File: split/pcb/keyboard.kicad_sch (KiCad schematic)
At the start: 116 parts, among them J1 TRRS, J2 IO

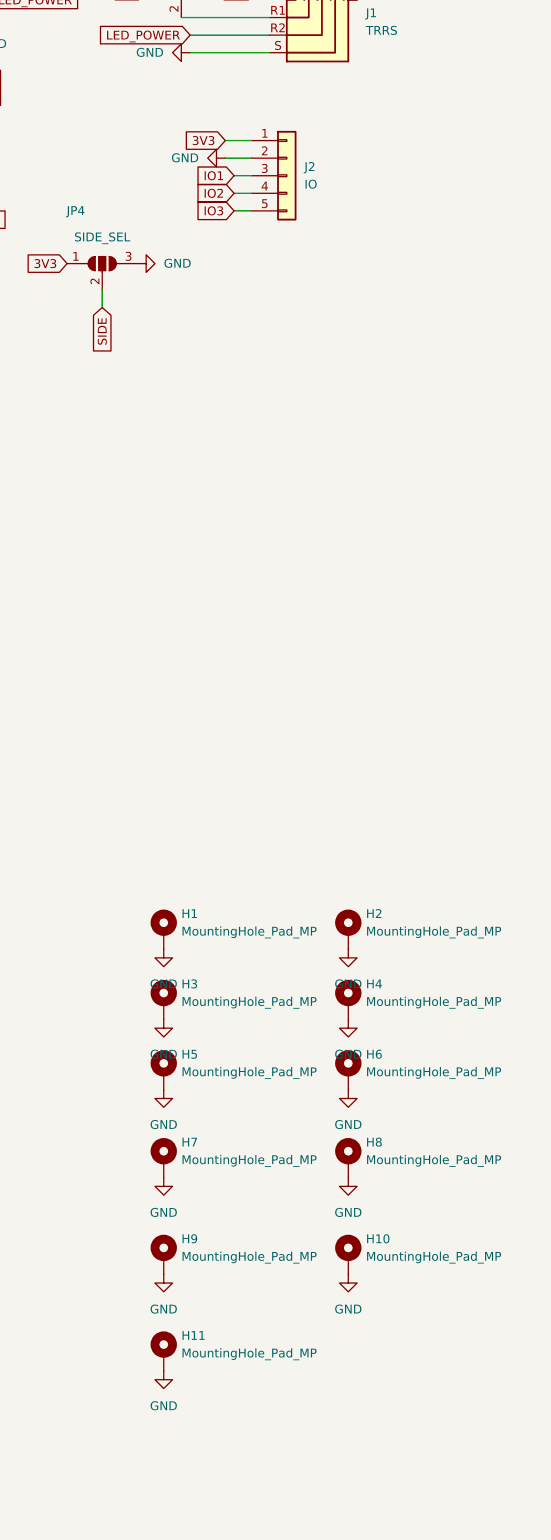
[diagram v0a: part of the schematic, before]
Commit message: fix accessory connector
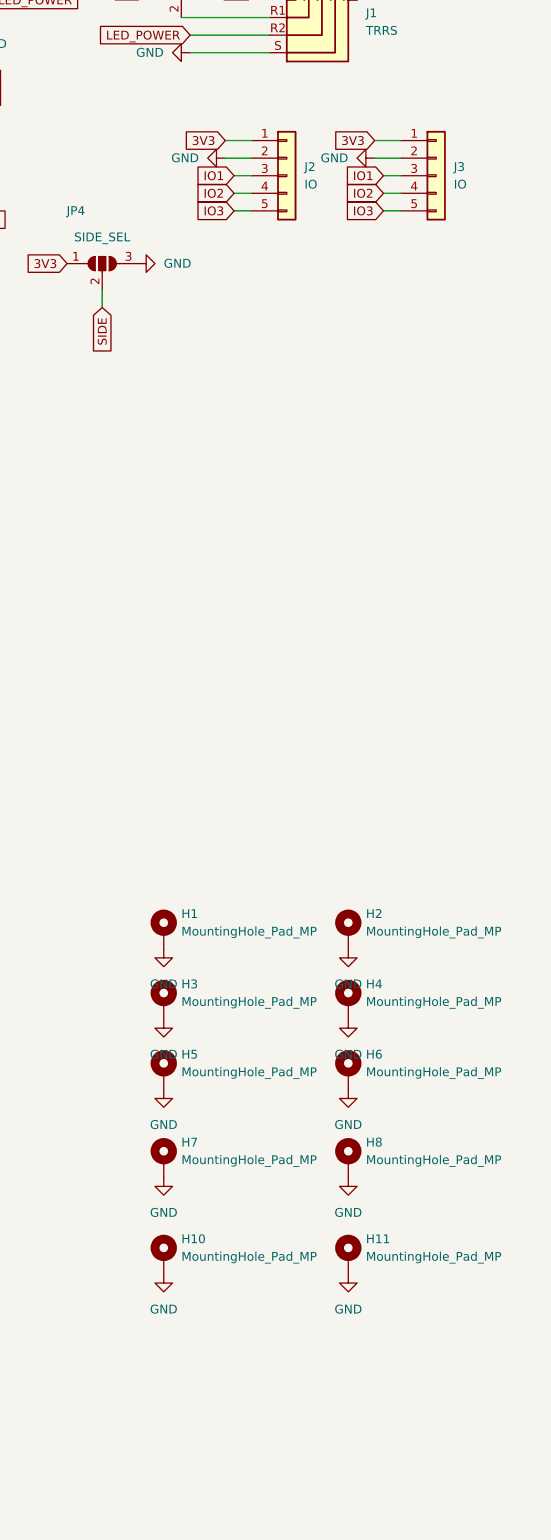
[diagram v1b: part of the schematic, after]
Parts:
- removed H9: MountingHole_Pad_MP, MountingHole:MountingHole_2.2mm_M2_DIN965_Pad, symbol Mechanical:MountingHole_Pad
- added J3: IO, Connector_PinHeader_2.54mm:PinHeader_1x05_P2.54mm_Vertical, symbol Connector_Generic:Conn_01x05
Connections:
- net 3V3: now also J3.1 (Pin_1)
- net GND: now also J3.2 (Pin_2)
- net IO1: now also J3.3 (Pin_3)
- net IO2: now also J3.4 (Pin_4)
- net IO3: now also J3.5 (Pin_5)
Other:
- moved on the sheet: H10, H11

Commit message: pcb fixes
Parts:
- removed JP2: T_SEL, Jumper:SolderJumper-3_P1.3mm_Open_Pad1.0x1.5mm, symbol Jumper:SolderJumper_3_Open
- removed JP3: R1_SEL, Jumper:SolderJumper-3_P1.3mm_Open_Pad1.0x1.5mm, symbol Jumper:SolderJumper_3_Open
- added JP1: SolderJumper_2_Open, Jumper:SolderJumper-2_P1.3mm_Open_Pad1.0x1.5mm, symbol Jumper:SolderJumper_2_Open
- J2, J3: footprint Connector_PinHeader_2.54mm:PinHeader_1x05_P2.54mm_Vertical -> Connector_PinHeader_2.54mm:PinHeader_1x07_P2.54mm_Vertical; symbol Connector_Generic:Conn_01x05 -> Connector_Generic:Conn_01x07
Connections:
- net GND: now also J2.3 (Pin_3), J3.3 (Pin_3), JP1.2 (B); no longer J2.2 (Pin_2), J3.2 (Pin_2)
- net IO1: now also J2.4 (Pin_4), J3.4 (Pin_4); no longer J2.3 (Pin_3), J3.3 (Pin_3)
- net IO2: now also J2.5 (Pin_5), J3.5 (Pin_5); no longer J2.4 (Pin_4), J3.4 (Pin_4)
- net IO3: now also J2.6 (Pin_6), J3.6 (Pin_6); no longer J2.5 (Pin_5), J3.5 (Pin_5)
- net LED_POWER: now also J2.2 (Pin_2), J3.2 (Pin_2)
- net RX: now also J1.R1
- net TX: now also J1.T
- net IO4: now reaches U1.23 (GP23)
- net IO4: now also J2.7 (Pin_7), J3.7 (Pin_7)
- net at U1.BOOT: now also JP1.1 (A)
- no-connect marks 12 -> 10
